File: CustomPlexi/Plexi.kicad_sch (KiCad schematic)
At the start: 13 parts, among them U1 TL074

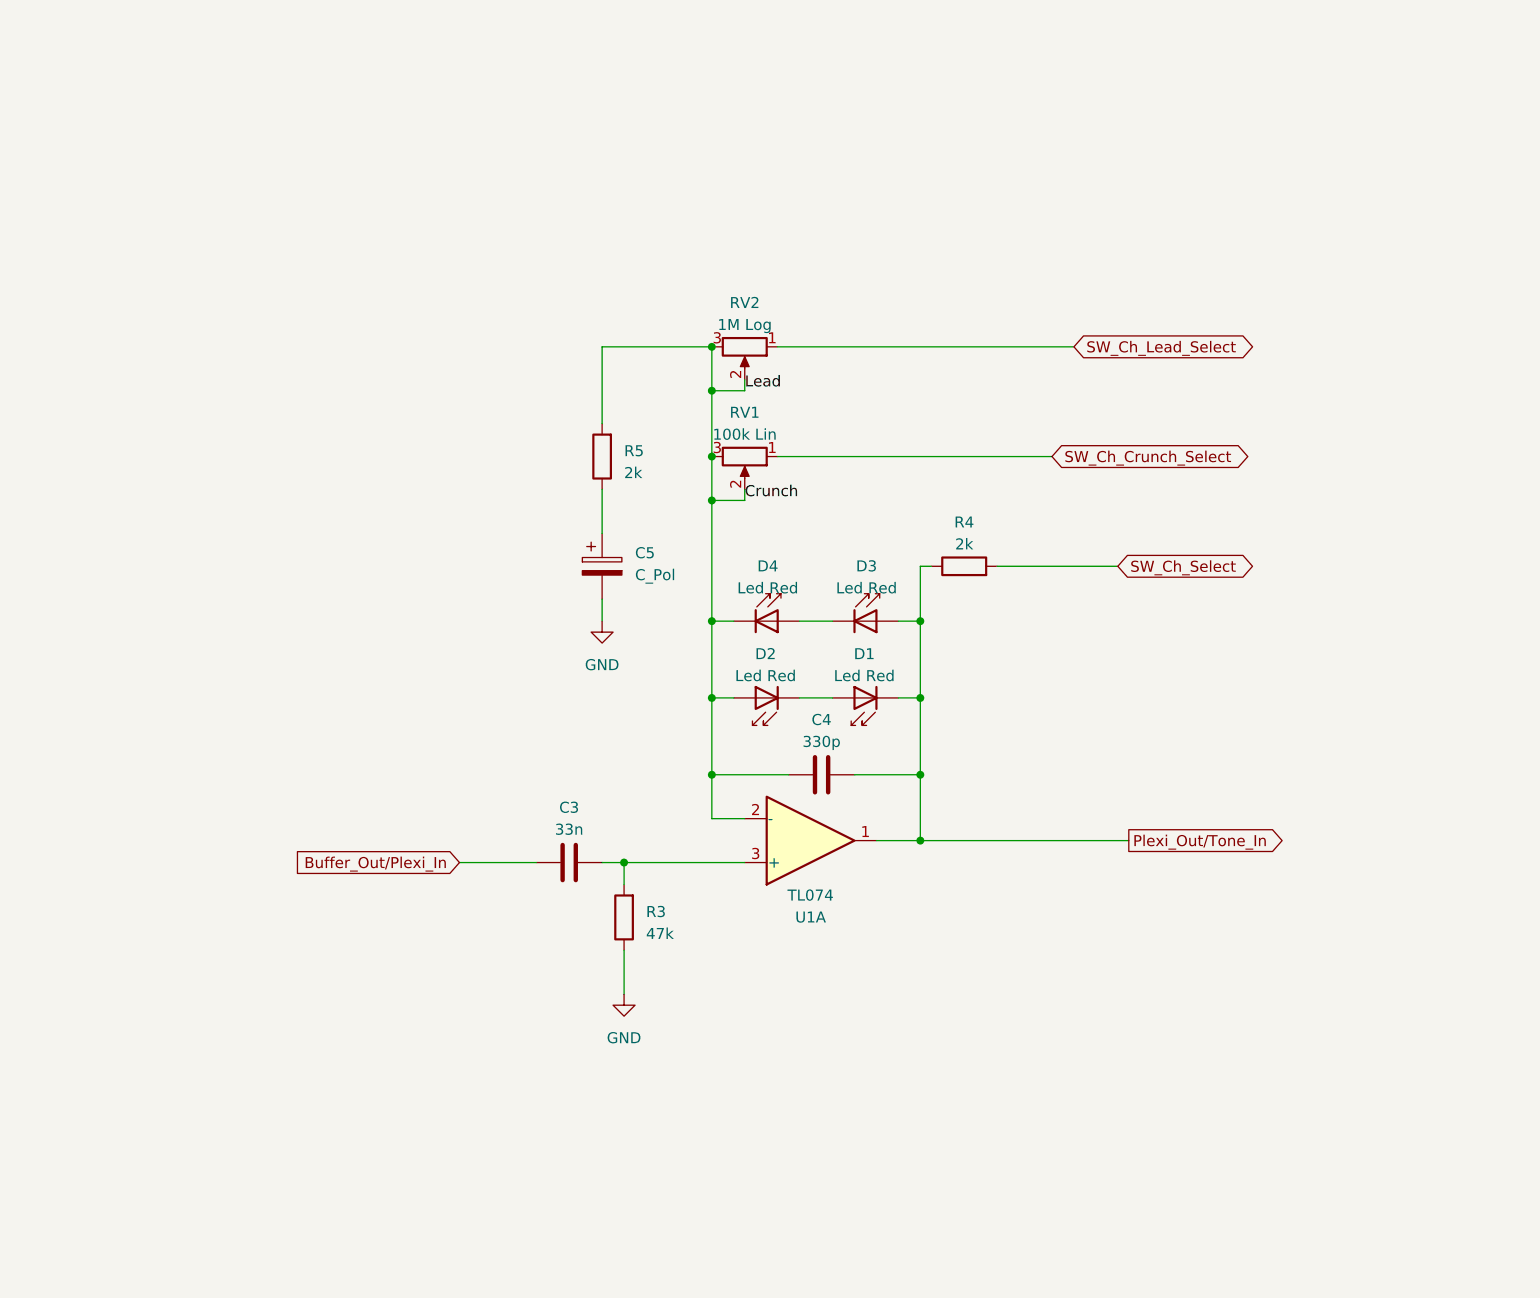
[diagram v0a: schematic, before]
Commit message: Signal chain ok except separated volumes
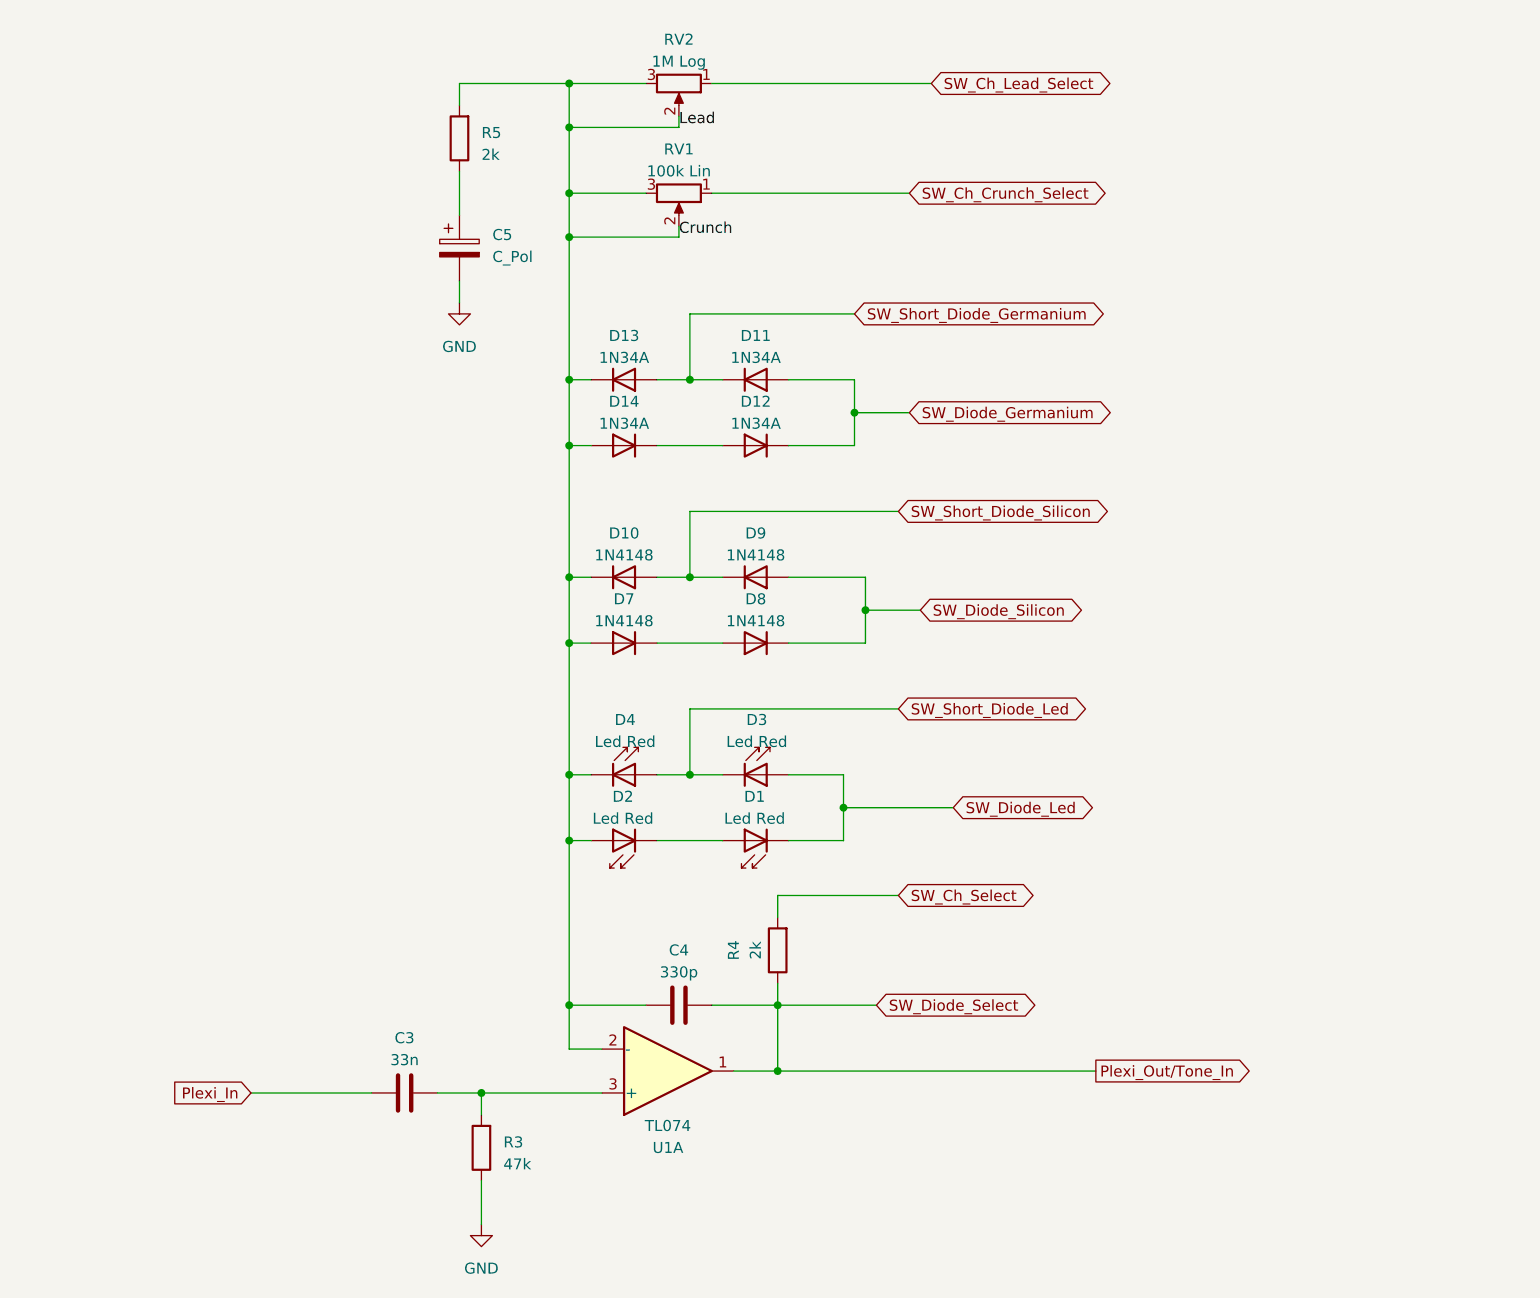
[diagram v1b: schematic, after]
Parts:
- added D10, D7, D8, D9: 1N4148, Diode_THT:D_DO-35_SOD27_P7.62mm_Horizontal, symbol Diode:1N4148
- added D11, D12, D13, D14: 1N34A, Diode_THT:D_DO-35_SOD27_P7.62mm_Horizontal, symbol Diode:1N4148
- C3, C4: footprint Capacitor_SMD:C_0603_1608Metric_Pad1.08x0.95mm_HandSolder -> Capacitor_SMD_AKL:C_0603_1608Metric
- R3, R4, R5: footprint Resistor_SMD:R_0603_1608Metric_Pad0.98x0.95mm_HandSolder -> Resistor_SMD_AKL:R_0603_1608Metric
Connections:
- net Crunch: now also D10.1 (K), D13.1 (K), D14.2 (A), D7.2 (A)
- net Plexi_Out/Tone_In: no longer D1.1 (K), D3.2 (A)
- net SW_Short_Diode_Led: now reaches D3.1 (K), D4.2 (A)
- net Buffer_Out/Plexi_In renamed Plexi_In
- new net: D12.2 (A), D14.1 (K)
- new net: D7.1 (K), D8.2 (A)
- new net SW_Diode_Germanium: D11.2 (A), D12.1 (K)
- new net SW_Diode_Led: D1.1 (K), D3.2 (A)
- new net SW_Diode_Silicon: D8.1 (K), D9.2 (A)
- new net SW_Short_Diode_Germanium: D11.1 (K), D13.2 (A)
- new net SW_Short_Diode_Silicon: D10.2 (A), D9.1 (K)
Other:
- moved on the sheet: C3, C4, C5, D1, D2, D3, D4, R3, R4, R5, RV1, RV2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

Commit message: some changes
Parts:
- added SW1: Diode Type, symbol Switch:SW_SP3T
- added SW2: Clipping Type, symbol CustomLib:SW_SPST_x3
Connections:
- net SW_Diode_Germanium: no longer names the net of D11.2 (A), D12.1 (K)
- net SW_Diode_Germanium: now also SW1.1, SW2.2
- net SW_Diode_Led: no longer names the net of D1.1 (K), D3.2 (A)
- net SW_Diode_Led: now also SW1.4, SW2.2
- net SW_Diode_Silicon: no longer names the net of D8.1 (K), D9.2 (A)
- net SW_Diode_Silicon: now also SW1.2, SW2.2
- net SW_Short_Diode_Germanium: no longer names the net of D11.1 (K), D13.2 (A)
- net SW_Short_Diode_Germanium: now also SW2.1
- net SW_Short_Diode_Led: no longer names the net of D3.1 (K), D4.2 (A)
- net SW_Short_Diode_Led: now also SW2.1
- net SW_Short_Diode_Silicon: no longer names the net of D10.2 (A), D9.1 (K)
- net SW_Short_Diode_Silicon: now also SW2.1
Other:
- moved on the sheet: D1, D11, D12, D13, D14, D2, D3, D4, RV1, RV2

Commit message: commit
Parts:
- added SW5: Plexi Channel Select, symbol CustomLib:SW_SPDT_x4
- RV1: value 100k Lin -> 1M Log
- RV2: value 1M Log -> 100k Lin
- SW1: value Diode Type -> Diode Select
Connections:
- net Plexi_Out/Tone_In: now also SW1.3
- net SW_Ch_Crunch_Select: no longer names the net of RV1.1
- net SW_Ch_Crunch_Select: now also SW5.3
- net SW_Ch_Lead_Select: no longer names the net of RV2.1
- net SW_Ch_Lead_Select: now also SW5.1
- net SW_Ch_Select: no longer names the net of R4.2
- net SW_Ch_Select: now also SW5.2
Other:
- moved on the sheet: C5, D1, D10, D11, D12, D13, D14, D2, D3, D4, D7, D8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

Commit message: switches reviewed
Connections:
- net Plexi_In renamed Preamp_Out/Plexi_In
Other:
- moved on the sheet: R4
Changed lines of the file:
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@@
     (stroke (width 0) (type default))
   )
-  (wire (pts (xy 165.1 73.66) (xy 165.1 95.25))
+  (wire (pts (xy 165.1 71.12) (xy 165.1 95.25))
     (stroke (width 0) (type default))
   )
@@
     (stroke (width 0) (type default))
   )
-  (wire (pts (xy 165.1 43.18) (xy 165.1 66.04))
+  (wire (pts (xy 165.1 43.18) (xy 165.1 63.5))
     (stroke (width 0) (type default))
   )
@@
     (effects (font (size 1.27 1.27)) (justify left bottom))
   )
-  (global_label "Plexi_In" (shape input) (at 73.66 151.13 180) (fields_autoplaced)
+  (global_label "Preamp_Out{slash}Plexi_In" (shape input) (at 73.66 151.13 180) (fields_autoplaced)
     (effects (font (size 1.27 1.27)) (justify right))
-    (property "Intersheetrefs" "${INTERSHEET_REFS}" (at 63.3761 151.13 0)
+    (property "Intersheetrefs" "${INTERSHEET_REFS}" (at 50.7367 151.13 0)
       (effects (font (size 1.27 1.27)) (justify right) hide)
     )
@@
     )
   )
-  (symbol (lib_id "PCM_Resistor_AKL:R_0603") (at 165.1 69.85 180) (unit 1)
-    (in_bom yes) (on_board yes) (dnp no)
-    (property "Reference" "R4" (at 160.02 69.85 90)
-      (effects (font (size 1.27 1.27)))
-    )
-    (property "Value" "2k" (at 162.56 69.85 90)
-      (effects (font (size 1.27 1.27)))
-    )
-    (property "Footprint" "Resistor_SMD_AKL:R_0603_1608Metric" (at 165.1 58.42 0)
-      (effects (font (size 1.27 1.27)) hide)
-    )
-    (property "Datasheet" "~" (at 165.1 69.85 0)
-      (effects (font (size 1.27 1.27)) hide)
-    )
+  (symbol (lib_id "PCM_Resistor_AKL:R_0603") (at 165.1 67.31 180) (unit 1)
+    (in_bom yes) (on_board yes) (dnp no)
+    (property "Reference" "R4" (at 160.02 67.31 90)
+      (effects (font (size 1.27 1.27)))
+    )
+    (property "Value" "2k" (at 162.56 67.31 90)
+      (effects (font (size 1.27 1.27)))
+    )
+    (property "Footprint" "Resistor_SMD_AKL:R_0603_1608Metric" (at 165.1 55.88 0)
+      (effects (font (size 1.27 1.27)) hide)
+    )
+    (property "Datasheet" "~" (at 165.1 67.31 0)
+      (effects (font (size 1.27 1.27)) hide)
+    )

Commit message: commit
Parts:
- C3, C4: footprint Capacitor_SMD_AKL:C_0603_1608Metric -> Capacitor_SMD:C_0402_1005Metric_Pad0.74x0.62mm_HandSolder
- R3, R4, R5: footprint Resistor_SMD_AKL:R_0603_1608Metric -> Resistor_SMD:R_0402_1005Metric_Pad0.72x0.64mm_HandSolder
- RV1, RV2: footprint (none) -> PCM_Potentiometer_THT_US_AKL_Double:Potentiometer_Vishay_148-149_Single_Vertical
- SW1, SW2: footprint (none) -> CustomLib:SW_SP3T_PinHeader2.54mm
- SW5: footprint (none) -> CustomLib:SW_SPST_x4_PinHeader2.54mm
- U1: footprint (none) -> Package_SO:SOIC-14W_7.5x9mm_P1.27mm
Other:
- moved on the sheet: C3, C4
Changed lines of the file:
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@@
   (junction (at 110.49 140.97) (diameter 0) (color 0 0 0 0)
   )
-  (junction (at 134.62 140.97) (diameter 0) (color 0 0 0 0)
-  )
   (junction (at 110.49 41.91) (diameter 0) (color 0 0 0 0)
   )
-  (junction (at 134.62 148.59) (diameter 0) (color 0 0 0 0)
+  (junction (at 165.1 140.97) (diameter 0) (color 0 0 0 0)
+  )
+  (junction (at 165.1 148.59) (diameter 0) (color 0 0 0 0)
   )
   (junction (at 110.49 95.25) (diameter 0) (color 0 0 0 0)
@@
     (stroke (width 0) (type default))
   )
-  (wire (pts (xy 73.66 151.13) (xy 87.63 151.13))
+  (wire (pts (xy 73.66 151.13) (xy 83.82 151.13))
     (stroke (width 0) (type default))
   )
@@
     (stroke (width 0) (type default))
   )
-  (wire (pts (xy 110.49 140.97) (xy 119.38 140.97))
+  (wire (pts (xy 110.49 140.97) (xy 130.81 140.97))
     (stroke (width 0) (type default))
   )
@@
     (stroke (width 0) (type default))
   )
-  (wire (pts (xy 134.62 140.97) (xy 134.62 148.59))
-    (stroke (width 0) (type default))
-  )
-  (wire (pts (xy 134.62 140.97) (xy 165.1 140.97))
-    (stroke (width 0) (type default))
-  )
   (wire (pts (xy 110.49 146.05) (xy 110.49 140.97))
     (stroke (width 0) (type default))
@@
     (stroke (width 0) (type default))
   )
-  (wire (pts (xy 95.25 151.13) (xy 100.33 151.13))
+  (wire (pts (xy 91.44 151.13) (xy 100.33 151.13))
     (stroke (width 0) (type default))
   )
@@
     (stroke (width 0) (type default))
   )
+  (wire (pts (xy 165.1 148.59) (xy 196.85 148.59))
+    (stroke (width 0) (type default))
+  )
   (wire (pts (xy 110.49 102.87) (xy 113.03 102.87))
     (stroke (width 0) (type default))
@@
     (stroke (width 0) (type default))
   )
-  (wire (pts (xy 134.62 148.59) (xy 129.54 148.59))
-    (stroke (width 0) (type default))
-  )
   (wire (pts (xy 135.89 69.85) (xy 140.97 69.85))
     (stroke (width 0) (type default))
@@
     (stroke (width 0) (type default))
   )
-  (wire (pts (xy 134.62 148.59) (xy 171.45 148.59))
+  (wire (pts (xy 129.54 148.59) (xy 165.1 148.59))
     (stroke (width 0) (type default))
   )
@@
     (stroke (width 0) (type default))
   )
-  (wire (pts (xy 127 140.97) (xy 134.62 140.97))
+  (wire (pts (xy 138.43 140.97) (xy 165.1 140.97))
     (stroke (width 0) (type default))
   )
@@
   )
   (wire (pts (xy 97.79 60.96) (xy 97.79 63.5))
+    (stroke (width 0) (type default))
+  )
+  (wire (pts (xy 165.1 140.97) (xy 165.1 148.59))
     (stroke (width 0) (type default))
   )
@@
     )
   )
-  (global_label "Plexi_Out{slash}Tone_In" (shape output) (at 171.45 148.59 0) (fields_autoplaced)
+  (global_label "Plexi_Out{slash}Tone_In" (shape output) (at 196.85 148.59 0) (fields_autoplaced)
     (effects (font (size 1.27 1.27)) (justify left))
-    (property "Intersheetrefs" "${INTERSHEET_REFS}" (at 191.5914 148.59 0)
+    (property "Intersheetrefs" "${INTERSHEET_REFS}" (at 216.9914 148.59 0)
       (effects (font (size 1.27 1.27)) (justify left) hide)
     )
@@
       (effects (font (size 1.27 1.27)) (justify right))
     )
-    (property "Footprint" "Resistor_SMD_AKL:R_0603_1608Metric" (at 97.79 33.02 0)
+    (property "Footprint" "Resistor_SMD:R_0402_1005Metric_Pad0.72x0.64mm_HandSolder" (at 97.79 33.02 0)
       (effects (font (size 1.27 1.27)) hide)
     )
@@
       (effects (font (size 1.27 1.27)))
     )
-    (property "Footprint" "" (at 120.65 151.13 0)
+    (property "Footprint" "Package_SO:SOIC-14W_7.5x9mm_P1.27mm" (at 120.65 151.13 0)
       (effects (font (size 1.27 1.27)) hide)
     )
@@
       (effects (font (size 1.27 1.27)))
     )
-    (property "Footprint" "" (at 123.19 36.83 0)
+    (property "Footprint" "PCM_Potentiometer_THT_US_AKL_Double:Potentiometer_Vishay_148-149_Single_Vertical" (at 123.19 36.83 0)
       (effects (font (size 1.27 1.27)) hide)
     )
@@
       (effects (font (size 1.27 1.27)))
     )
-    (property "Footprint" "Resistor_SMD_AKL:R_0603_1608Metric" (at 165.1 55.88 0)
+    (property "Footprint" "Resistor_SMD:R_0402_1005Metric_Pad0.72x0.64mm_HandSolder" (at 165.1 55.88 0)
       (effects (font (size 1.27 1.27)) hide)
     )
@@
       (effects (font (size 1.27 1.27)))
     )
-    (property "Footprint" "" (at 128.27 110.49 0)
+    (property "Footprint" "CustomLib:SW_SP3T_PinHeader2.54mm" (at 128.27 110.49 0)
       (effects (font (size 1.27 1.27)) hide)
     )
@@
     )
   )
-  (symbol (lib_id "PCM_Capacitor_AKL:C_0603") (at 123.19 140.97 90) (unit 1)
-    (in_bom yes) (on_board yes) (dnp no)
-    (property "Reference" "C4" (at 123.19 134.62 90)
-      (effects (font (size 1.27 1.27)))
-    )
-    (property "Value" "330p" (at 123.19 137.16 90)
-      (effects (font (size 1.27 1.27)))
-    )
-    (property "Footprint" "Capacitor_SMD_AKL:C_0603_1608Metric" (at 127 140.0048 0)
-      (effects (font (size 1.27 1.27)) hide)
-    )
-    (property "Datasheet" "~" (at 123.19 140.97 0)
+  (symbol (lib_id "PCM_Capacitor_AKL:C_0603") (at 134.62 140.97 90) (unit 1)
+    (in_bom yes) (on_board yes) (dnp no)
+    (property "Reference" "C4" (at 134.62 134.62 90)
+      (effects (font (size 1.27 1.27)))
+    )
+    (property "Value" "330p" (at 134.62 137.16 90)
+      (effects (font (size 1.27 1.27)))
+    )
+    (property "Footprint" "Capacitor_SMD:C_0402_1005Metric_Pad0.74x0.62mm_HandSolder" (at 138.43 140.0048 0)
+      (effects (font (size 1.27 1.27)) hide)
+    )
+    (property "Datasheet" "~" (at 134.62 140.97 0)
       (effects (font (size 1.27 1.27)) hide)
     )
@@
       (effects (font (size 1.27 1.27)))
     )
-    (property "Footprint" "" (at 152.4 38.1 0)
+    (property "Footprint" "CustomLib:SW_SPST_x4_PinHeader2.54mm" (at 152.4 38.1 0)
       (effects (font (size 1.27 1.27)) hide)
     )
@@
       (effects (font (size 1.27 1.27)))
     )
-    (property "Footprint" "" (at 128.27 86.36 0)
+    (property "Footprint" "CustomLib:SW_SP3T_PinHeader2.54mm" (at 128.27 86.36 0)
       (effects (font (size 1.27 1.27)) hide)
     )
@@
       (effects (font (size 1.27 1.27)) (justify right))
     )
-    (property "Footprint" "Resistor_SMD_AKL:R_0603_1608Metric" (at 100.33 146.05 0)
+    (property "Footprint" "Resistor_SMD:R_0402_1005Metric_Pad0.72x0.64mm_HandSolder" (at 100.33 146.05 0)
       (effects (font (size 1.27 1.27)) hide)
     )
@@
       (effects (font (size 1.27 1.27)))
     )
-    (property "Footprint" "" (at 172.085 90.805 0)
+    (property "Footprint" "CustomLib:SW_SP3T_PinHeader2.54mm" (at 172.085 90.805 0)
       (effects (font (size 1.27 1.27)) hide)
     )
@@
       (effects (font (size 1.27 1.27)))
     )
-    (property "Footprint" "" (at 129.54 60.96 0)
+    (property "Footprint" "CustomLib:SW_SP3T_PinHeader2.54mm" (at 129.54 60.96 0)
       (effects (font (size 1.27 1.27)) hide)
     )
@@
     )
   )
-  (symbol (lib_id "PCM_Capacitor_AKL:C_0603") (at 91.44 151.13 90) (unit 1)
-    (in_bom yes) (on_board yes) (dnp no) (fields_autoplaced)
-    (property "Reference" "C3" (at 91.44 144.78 90)
-      (effects (font (size 1.27 1.27)))
-    )
-    (property "Value" "33n" (at 91.44 147.32 90)
-      (effects (font (size 1.27 1.27)))
-    )
-    (property "Footprint" "Capacitor_SMD_AKL:C_0603_1608Metric" (at 95.25 150.1648 0)
-      (effects (font (size 1.27 1.27)) hide)
-    )
-    (property "Datasheet" "~" (at 91.44 151.13 0)
+  (symbol (lib_id "PCM_Capacitor_AKL:C_0603") (at 87.63 151.13 90) (unit 1)
+    (in_bom yes) (on_board yes) (dnp no) (fields_autoplaced)
+    (property "Reference" "C3" (at 87.63 144.78 90)
+      (effects (font (size 1.27 1.27)))
+    )
+    (property "Value" "33n" (at 87.63 147.32 90)
+      (effects (font (size 1.27 1.27)))
+    )
+    (property "Footprint" "Capacitor_SMD:C_0402_1005Metric_Pad0.74x0.62mm_HandSolder" (at 91.44 150.1648 0)
+      (effects (font (size 1.27 1.27)) hide)
+    )
+    (property "Datasheet" "~" (at 87.63 151.13 0)
       (effects (font (size 1.27 1.27)) hide)
     )
@@
       (effects (font (size 1.27 1.27)))
     )
-    (property "Footprint" "" (at 123.19 49.53 0)
-      (effects (font (size 1.27 1.27)) hide)
-    )
+    (property "Footprint" "PCM_Potentiometer_THT_US_AKL_Double:Potentiometer_Vishay_148-149_Single_Vertical" (at 123.19 49.53 0)
+      (effects (font (size 1.27 1.27)) hide)
+    )

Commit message: changed refdes
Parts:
- renumbered D11 to D10, D12 to D11, D9 to D12, D8 to D13, D13 to D4, D14 to D5, D10 to D6, SW2 to SW4, SW1 to SW6
